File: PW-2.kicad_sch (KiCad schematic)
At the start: 10 parts, among them J1 Conn_01x02_Male, J2 Conn_01x02_Female, Q1 BSC025N08LS5

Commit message: many
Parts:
- removed Q1: BSC025N08LS5, Package_TO_SOT_SMD:TDSON-8-1, symbol Transistor_FET_additional:BSC025N08LS5
- added C12: 10u, Capacitor_SMD:C_0805_2012Metric, symbol Device:C
- added C13, C16, C19, C20, C21, C22, C23, C24, C25: 100n, Capacitor_SMD:C_0603_1608Metric, symbol Device:C
- added C14, C15: 22p, Capacitor_SMD:C_0603_1608Metric, symbol Device:C
- added C17, C18: 1u, Capacitor_SMD:C_0603_1608Metric, symbol Device:C
- added D2: D_TVS, Diode_SMD:D_SMA, symbol Device:D_TVS
- added D3: LED, Resistor_SMD:R_0603_1608Metric, symbol Device:LED
- added D4, D5, D6, D7: WS2812C, LED_additional:LED_2020Metric_WS2812C_2.0x2.0mm_P1.0mm, symbol LED_additional:WS2812C
- added J5: Conn_02x07_Odd_Even, Connector_PinHeader_1.27mm:PinHeader_2x07_P1.27mm_Vertical_SMD, symbol Connector_Generic:Conn_02x07_Odd_Even
- added J6, J7: Conn_01x04_Female, Connector_JST:JST_XA_S04B-XASK-1_1x04_P2.50mm_Horizontal, symbol Connector:Conn_01x04_Female
- added JP1: SolderJumper_3_Bridged12, Jumper:SolderJumper-3_P1.3mm_Bridged12_RoundedPad1.0x1.5mm, symbol Jumper:SolderJumper_3_Bridged12
- added Q1: IPT007N06N, Package_TO_SOT_SMD:Infineon_PG-HSOF-8-1_ThermalVias, symbol Transistor_FET_additional:IPT007N06N
- added R14, R15, R16: 10k, Resistor_SMD:R_0603_1608Metric, symbol Device:R
- added R17: 120, Resistor_SMD:R_0603_1608Metric, symbol Device:R
- added SW1: SW_Push, Button_Switch_additional:TVAF06-A020B-R, symbol Switch:SW_Push
- added SW2: SW_SPDT, Button_Switch_additional:IS-1245T-G, symbol Switch:SW_SPDT
- added U3: L78L12_SOT89, Package_TO_SOT_SMD:SOT-89-3, symbol Regulator_Linear:L78L12_SOT89
- added U4: MCP1700-3302E_SOT23, Package_TO_SOT_SMD:SOT-23, symbol Regulator_Linear:MCP1700-3302E_SOT23
- added U5: STM32F303K8Tx, Package_QFP:LQFP-32_7x7mm_P0.8mm, symbol MCU_ST_STM32F3:STM32F303K8Tx
- added U6: IM920s, interplan:IM920s, symbol interplan:IM920s
- added U7: MCP2551-I-SN, Package_SO:SOIC-8_3.9x4.9mm_P1.27mm, symbol Interface_CAN_LIN:MCP2551-I-SN
- added Y1: 16MHz, Crystal:Crystal_SMD_HC49-SD, symbol Device:Crystal
- F1, F2, F3, F4: footprint (none) -> Fuse_additional:Fuseholder_Keystone_3568
- gave numbers to parts that had none: 2
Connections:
- net +5V: now also C17.2, C20.2, C21.2, C22.2, C23.2, C25.2, D4.4 (VDD), D5.4 (VDD), D6.4 (VDD), D7.4 (VDD), U4.3 (VI), U7.3 (VDD)
- net +BATT: now also C12.1, U3.3 (IN)
- net GND: now also C14.1, C15.1, C16.1, C17.1, C18.1, C19.1, C20.1, C21.1, C22.1, C23.1, C24.1, C25.1, D4.2 (VSS), D5.2 (VSS), D6.2 (VSS), D7.2 (VSS), J5.11 (Pin_11), J5.5 (Pin_5), J5.7 (Pin_7), JP1.1 (A), R15.1, R16.1, SW1.1, U4.1 (GND), U5.16 (VSS), U5.32 (VSS), U6.18 (GND), U7.2 (VSS)
- net GNDPWR: now also C12.2, C13.1, D2.1 (A1), Q1.2 (S), U3.2 (GND)
- net Vout-: now also Q1.3 (D)
- net main_breaker_gate: now also Q1.1 (G)
- net at F1.2, FL1.1 (B): now also D2.2 (A2)
- new net: C15.2, U5.3 (PF1), Y1.1
- new net: D3.1 (K), R15.2
- new net: JP1.2 (C), R14.1
- new net: D5.1 (DOUT), D6.3 (DIN)
- new net: D4.1 (DOUT), D5.3 (DIN)
- new net: D3.2 (A), U6.15 (STATUS)
- new net: R14.2, U5.31 (BOOT0)
- new net: R16.2, U7.8 (Rs)
- new net: R17.1, SW2.2 (B)
- new net: C14.2, U5.2 (PF0), Y1.2
- new net: D6.1 (DOUT), D7.3 (DIN)
- new net +12P: C13.2, U3.1 (OUT)
- new net +3V3: C18.2, C19.2, C24.2, J5.3 (Pin_3), JP1.3 (B), U4.2 (VO), U5.1 (VDD), U5.17 (VDD), U5.5 (VDDA), U6.17 (VCC)
- new net CANH: J6.2 (Pin_2), J7.2 (Pin_2), SW2.1 (A), U7.7 (CANH)
- new net CANL: J6.3 (Pin_3), J7.3 (Pin_3), R17.2, U7.6 (CANL)
- new net CAN_RX: U5.21 (PA11), U7.4 (RXD)
- new net CAN_TX: U5.22 (PA12), U7.1 (TXD)
- new net IM920_IO1: U5.6 (PA0), U6.1 (IO1/BUSY)
- new net IM920_IO10: U5.18 (PA8), U6.10 (IO10)
- new net IM920_IO2: U5.7 (PA1), U6.2 (IO2)
- new net IM920_IO3: U5.11 (PA5), U6.3 (IO3/XMIT)
- new net IM920_IO4: U5.12 (PA6), U6.4 (IO4/SLEEP)
- new net IM920_IO5: U5.10 (PA4), U6.5 (IO5)
- new net IM920_IO6: U5.8 (PA2), U6.6 (IO6/RxD)
- new net IM920_IO7: U5.9 (PA3), U6.7 (IO7/TxD)
- new net IM920_IO8: U5.13 (PA7), U6.8 (IO8)
- new net NRST: C16.2, J5.12 (Pin_12), SW1.2, U5.4 (NRST)
- new net NeoPixel: D4.3 (DIN), U5.15 (PB1)
- new net SWCLK: J5.6 (Pin_6), U5.24 (PA14)
- new net SWDIO: J5.4 (Pin_4), U5.23 (PA13)
- new net VCP_RX: J5.13 (Pin_13), U5.19 (PA9)
- new net VCP_TX: J5.14 (Pin_14), U5.20 (PA10)
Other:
- moved on the sheet: F1, F2, F3, F4, FL1, J1, J2, J3, J4

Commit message: some
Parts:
- removed J4: USB_A_Stacked, Connector_USB:USB_A_Wuerth_61400826021_Horizontal_Stacked, symbol Connector:USB_A_Stacked
- added H1, H2, H3, H4: MountingHole, MountingHole:MountingHole_3.2mm_M3_Pad_Via, symbol Mechanical:MountingHole
- added J10, J11, J12, J13, J9: Conn_01x02_Male, Connector_PinHeader_2.54mm:PinHeader_1x02_P2.54mm_Vertical, symbol Connector:Conn_01x02_Male
- added J14, J15, J16, J17, J18, J19, J20: Conn_01x02_Female, Connector_JST:JST_XA_S02B-XASK-1_1x02_P2.50mm_Horizontal, symbol Connector:Conn_01x02_Female
- added J8: Conn_01x02_Female, Connector_T_connector:T_connecter_female_horizontal, symbol Connector:Conn_01x02_Female
- added JP2, JP3, JP4, JP5, JP6: SolderJumper_2_Open, Jumper:SolderJumper-2_P1.3mm_Open_RoundedPad1.0x1.5mm, symbol Jumper:SolderJumper_2_Open
- added R18: 10, Resistor_SMD:R_0603_1608Metric, symbol Device:R
- added R19: 330, Resistor_SMD:R_0603_1608Metric, symbol Device:R
- added SW3: SW_SPDT, Button_Switch_additional:IS-1245T-G, symbol Switch:SW_SPDT
- added U8: TLP152, Package_SO_additional:SO-6_5pin_4.4x3.6mm_P1.27mm, symbol Isolator_additional:TLP152
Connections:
- net +12P: now also U8.6
- net +5V: now also J18.1 (Pin_1), J19.1 (Pin_1), J20.1 (Pin_1)
- net GND: now also J10.2 (Pin_2), J11.2 (Pin_2), J12.2 (Pin_2), J13.2 (Pin_2), J14.2 (Pin_2), J15.2 (Pin_2), J16.2 (Pin_2), J17.2 (Pin_2), J18.2 (Pin_2), J19.2 (Pin_2), J20.2 (Pin_2), J9.2 (Pin_2), JP2.2 (B), JP3.2 (B), JP4.2 (B), JP5.2 (B), JP6.2 (B), SW3.1 (A), U8.3
- net GNDPWR: now also U8.4
- net IM920_IO10: now also U5.13 (PA7); no longer U5.18 (PA8)
- net IM920_IO3: now also U5.9 (PA3); no longer U5.11 (PA5)
- net IM920_IO4: now also U5.10 (PA4); no longer U5.12 (PA6)
- net IM920_IO5: now also U5.11 (PA5); no longer U5.10 (PA4)
- net IM920_IO6: now also U5.19 (PA9); no longer U5.8 (PA2)
- net IM920_IO7: now also U5.20 (PA10); no longer U5.9 (PA3)
- net IM920_IO8: now also U5.12 (PA6); no longer U5.13 (PA7)
- net VCP_RX: now also U5.25 (PA15); no longer U5.19 (PA9)
- net VCP_TX: now also U5.8 (PA2); no longer U5.20 (PA10)
- net Vout+: now also J8.1 (Pin_1)
- net Vout-: now also J8.2 (Pin_2)
- net main_breaker_gate: now also R18.2, U8.5; no longer Q1.1 (G)
- net IM920_RESET: now reaches U6.19 (RESET)
- net IM920_RESET: now also U5.18 (PA8)
- net breaker_signal: now reaches U5.14 (PB0)
- net breaker_signal: now also R19.2
- net disable_remote_kill: now reaches U5.26 (PB3)
- net disable_remote_kill: now also J9.1 (Pin_1), JP2.1 (A)
- net SW_IN1: now reaches U5.27 (PB4)
- net SW_IN1: now also J10.1 (Pin_1), J14.1 (Pin_1), JP3.1 (A), SW3.2 (B)
- net SW_IN2: now reaches U5.28 (PB5)
- net SW_IN2: now also J11.1 (Pin_1), J15.1 (Pin_1), JP4.1 (A)
- net SW_IN3: now reaches U5.29 (PB6)
- net SW_IN3: now also J12.1 (Pin_1), J16.1 (Pin_1), JP5.1 (A)
- net SW_IN4: now reaches U5.30 (PB7)
- net SW_IN4: now also J13.1 (Pin_1), J17.1 (Pin_1), JP6.1 (A)
- new net: Q1.1 (G), R18.1
- new net: R19.1, U8.1
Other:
- moved on the sheet: C12, C13, C14, C15, J5, U3, Y1

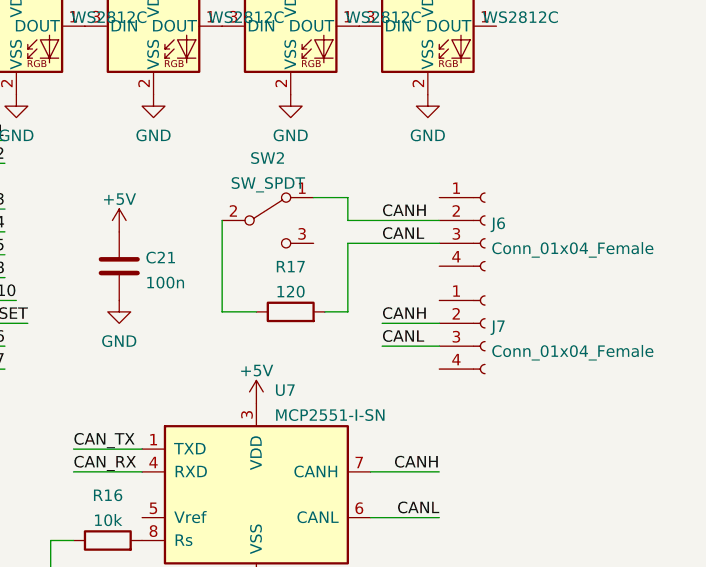
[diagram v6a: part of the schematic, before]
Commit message: drawing around power done
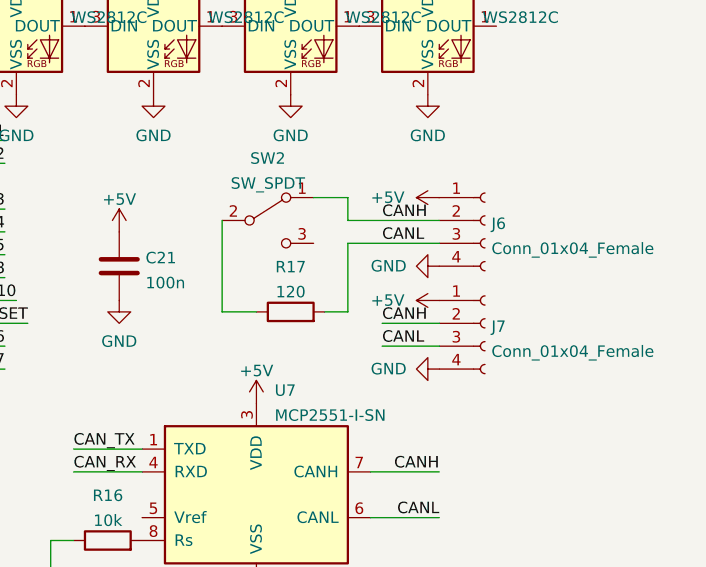
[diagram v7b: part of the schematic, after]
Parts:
- Q1: footprint Package_TO_SOT_SMD:Infineon_PG-HSOF-8-1_ThermalVias -> Package_TO_SOT_SMD:Infineon_PG-HSOF-8-1
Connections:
- net +5V: now also J6.1 (Pin_1), J7.1 (Pin_1)
- net GND: now also J6.4 (Pin_4), J7.4 (Pin_4)
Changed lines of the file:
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@@
     (pin "2")
+  )
+  (symbol (lib_id "power:GND") (at 273.05 80.01 270) (unit 1)
+    (in_bom yes) (on_board yes)
+    (property "Reference" "#PWR?" (id 0) (at 266.7 80.01 0)
+      (effects (font (size 1.27 1.27)) hide)
+    )
+    (property "Value" "GND" (id 1) (at 265.43 80.01 90)
+      (effects (font (size 1.27 1.27)) (justify left))
+    )
+    (property "Footprint" "" (id 2) (at 273.05 80.01 0)
+      (effects (font (size 1.27 1.27)) hide)
+    )
+    (property "Datasheet" "" (id 3) (at 273.05 80.01 0)
+      (effects (font (size 1.27 1.27)) hide)
+    )
+    (pin "1")
   )
   (symbol (lib_id "Device:Fuse") (at 59.69 48.26 90) (unit 1)
@@
     (pin "1")
   )
+  (symbol (lib_id "power:+5V") (at 273.05 72.39 90) (unit 1)
+    (in_bom yes) (on_board yes)
+    (property "Reference" "#PWR?" (id 0) (at 276.86 72.39 0)
+      (effects (font (size 1.27 1.27)) hide)
+    )
+    (property "Value" "+5V" (id 1) (at 265.43 72.39 90)
+      (effects (font (size 1.27 1.27)) (justify right))
+    )
+    (property "Footprint" "" (id 2) (at 273.05 72.39 0)
+      (effects (font (size 1.27 1.27)) hide)
+    )
+    (property "Datasheet" "" (id 3) (at 273.05 72.39 0)
+      (effects (font (size 1.27 1.27)) hide)
+    )
+    (pin "1")
+  )
   (symbol (lib_id "Connector:Conn_01x02_Female") (at 88.9 49.53 0) (unit 1)
     (in_bom yes) (on_board yes) (fields_autoplaced)
@@
       (effects (font (size 1.27 1.27)) hide)
     )
+  )
+  (symbol (lib_id "power:+5V") (at 273.05 60.96 90) (unit 1)
+    (in_bom yes) (on_board yes)
+    (property "Reference" "#PWR?" (id 0) (at 276.86 60.96 0)
+      (effects (font (size 1.27 1.27)) hide)
+    )
+    (property "Value" "+5V" (id 1) (at 265.43 60.96 90)
+      (effects (font (size 1.27 1.27)) (justify right))
+    )
+    (property "Footprint" "" (id 2) (at 273.05 60.96 0)
+      (effects (font (size 1.27 1.27)) hide)
+    )
+    (property "Datasheet" "" (id 3) (at 273.05 60.96 0)
+      (effects (font (size 1.27 1.27)) hide)
+    )
+    (pin "1")
   )
   (symbol (lib_id "Device:C") (at 276.86 22.86 180) (unit 1)
@@
     (pin "1")
   )
+  (symbol (lib_id "power:GND") (at 273.05 68.58 270) (unit 1)
+    (in_bom yes) (on_board yes)
+    (property "Reference" "#PWR?" (id 0) (at 266.7 68.58 0)
+      (effects (font (size 1.27 1.27)) hide)
+    )
+    (property "Value" "GND" (id 1) (at 265.43 68.58 90)
+      (effects (font (size 1.27 1.27)) (justify left))
+    )
+    (property "Footprint" "" (id 2) (at 273.05 68.58 0)
+      (effects (font (size 1.27 1.27)) hide)
+    )
+    (property "Datasheet" "" (id 3) (at 273.05 68.58 0)
+      (effects (font (size 1.27 1.27)) hide)
+    )
+    (pin "1")
+  )
   (symbol (lib_id "Device:R") (at 106.68 77.47 90) (unit 1)
     (in_bom yes) (on_board yes) (fields_autoplaced)
@@
     (property "Reference" "Q1" (id 0) (at 59.69 61.4385 90))
     (property "Value" "IPT007N06N" (id 1) (at 59.69 64.2136 90))
-    (property "Footprint" "Package_TO_SOT_SMD:Infineon_PG-HSOF-8-1_ThermalVias" (id 2) (at 59.69 67.31 0)
+    (property "Footprint" "Package_TO_SOT_SMD:Infineon_PG-HSOF-8-1" (id 2) (at 59.69 67.31 0)
       (effects (font (size 1.27 1.27)) hide)
     )
@@
       (reference "#PWR0108") (unit 1) (value "GND") (footprint "")
     )
+    (path "/111acb24-8fc7-4335-afac-cdae01c8fa5b"
+      (reference "#PWR?") (unit 1) (value "GND") (footprint "")
+    )
+    (path "/4ec356dc-2ab8-4016-a531-e41cd4934502"
+      (reference "#PWR?") (unit 1) (value "+5V") (footprint "")
+    )
+    (path "/7119ff1d-9b7c-4a49-9306-dec144374f02"
+      (reference "#PWR?") (unit 1) (value "+5V") (footprint "")
+    )
+    (path "/a82bda66-4ef5-4c21-b81e-72426982563f"
+      (reference "#PWR?") (unit 1) (value "GND") (footprint "")
+    )
     (path "/823bdb72-b3da-47c7-8be1-d919cd2d99f3/a3ba4a17-7310-4e11-bf4f-c2894df162a5"
       (reference "C1") (unit 1) (value "10u") (footprint "Capacitor_SMD:C_0805_2012Metric")
@@
     )
     (path "/cdc2bdba-c809-426a-ace6-469014406523"
-      (reference "Q1") (unit 1) (value "IPT007N06N") (footprint "Package_TO_SOT_SMD:Infineon_PG-HSOF-8-1_ThermalVias")
+      (reference "Q1") (unit 1) (value "IPT007N06N") (footprint "Package_TO_SOT_SMD:Infineon_PG-HSOF-8-1")
     )
     (path "/823bdb72-b3da-47c7-8be1-d919cd2d99f3/3aec649b-7bfb-45b0-aab7-a7fd1c3cd2bb"

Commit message: v0 done!
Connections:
- net CANH: now also SW2.3 (C); no longer SW2.1 (A)
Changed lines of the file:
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@@
+    (stroke (width 0) (type default) (color 0 0 0 0))
+  )
+  (wire (pts (xy 260.35 63.5) (xy 260.35 66.04))
     (stroke (width 0) (type default) (color 0 0 0 0))
   )
@@
     (stroke (width 0) (type default) (color 0 0 0 0))
   )
-  (wire (pts (xy 259.08 60.96) (xy 262.89 60.96))
-    (stroke (width 0) (type default) (color 0 0 0 0))
-  )
   (wire (pts (xy 181.61 123.19) (xy 187.96 123.19))
     (stroke (width 0) (type default) (color 0 0 0 0))
@@
     (stroke (width 0) (type default) (color 0 0 0 0))
   )
-  (wire (pts (xy 262.89 60.96) (xy 262.89 63.5))
-    (stroke (width 0) (type default) (color 0 0 0 0))
-  )
   (wire (pts (xy 161.29 105.41) (xy 153.67 105.41))
     (stroke (width 0) (type default) (color 0 0 0 0))
@@
     (stroke (width 0) (type default) (color 0 0 0 0))
   )
+  (wire (pts (xy 260.35 66.04) (xy 259.08 66.04))
+    (stroke (width 0) (type default) (color 0 0 0 0))
+  )
   (wire (pts (xy 177.8 45.72) (xy 186.69 45.72))
     (stroke (width 0) (type default) (color 0 0 0 0))
@@
     (stroke (width 0) (type default) (color 0 0 0 0))
   )
-  (wire (pts (xy 262.89 63.5) (xy 273.05 63.5))
-    (stroke (width 0) (type default) (color 0 0 0 0))
-  )
+  (wire (pts (xy 260.35 63.5) (xy 273.05 63.5))
+    (stroke (width 0) (type default) (color 0 0 0 0))
+  )
